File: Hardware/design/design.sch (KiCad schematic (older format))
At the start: 69 parts, among them SW1 NKK_NR01, SW10 NKK_NR01, SW11 SW_Push, SW12 SW_Push, SW13 SW_Push, SW14 SW_Push, SW15 NKK_NR01, SW16 SW_Push, SW17 SW_Push, SW18 SW_Push, SW19 SW_Push, SW2 SW_Push, SW20 NKK_NR01, SW21 SW_Push, SW22 SW_Push, SW23 SW_Push, SW24 SW_Push, SW25 SW_Push, SW26 SW_Push, SW27 SW_Push, SW28 SW_Push, SW3 SW_Push, SW4 SW_Push, SW5 SW_Push, SW6 SW_Push, SW7 SW_Push, SW8 SW_Push, SW9 SW_Push, U1 ProMicro

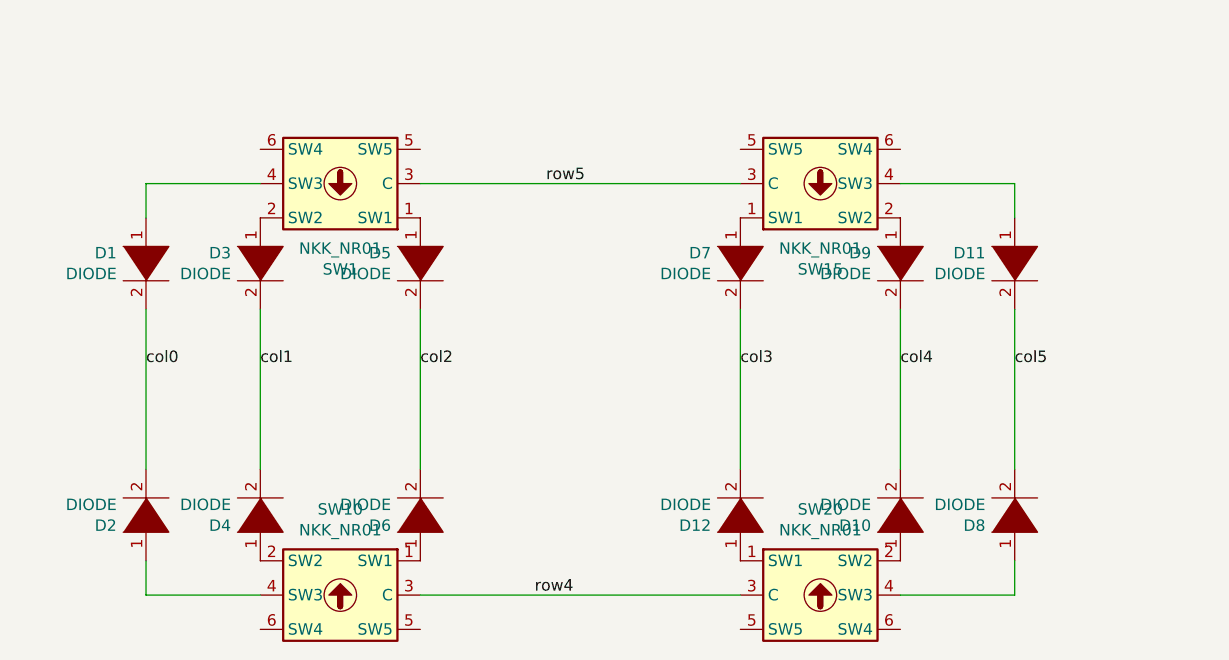
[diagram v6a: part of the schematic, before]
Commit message: routed all cherry switches and pots, fixed issue with rotary switch nets in schematic
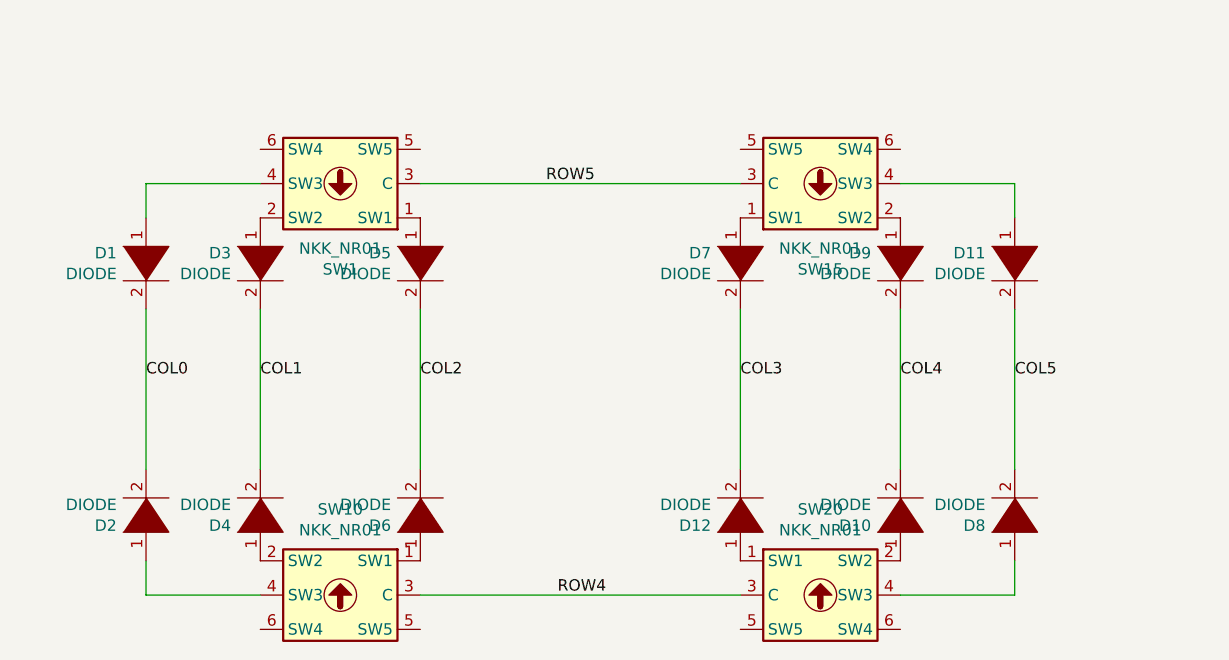
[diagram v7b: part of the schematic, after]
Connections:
- net labels removed: col0, col1, col2, col3, col4, col5, row4, row5
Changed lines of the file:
@@
 	1    0    0    -1
 $EndComp
-Text Label 3000 7100 0    50   ~ 0
-row4
 Wire Wire Line
 	5100 7100 5100 6950
@@
 	1300 5850 1300 6550
 Text Label 3050 5300 0    50   ~ 0
-row5
-Text Label 1300 6100 0    50   ~ 0
-col0
-Text Label 1800 6100 0    50   ~ 0
-col1
-Text Label 2500 6100 0    50   ~ 0
-col2
-Text Label 3900 6100 0    50   ~ 0
-col3
-Text Label 4600 6100 0    50   ~ 0
-col4
-Text Label 5100 6100 0    50   ~ 0
-col5
+ROW5
+Text Label 3100 7100 0    50   ~ 0
+ROW4
+Text Label 1300 6150 0    50   ~ 0
+COL0
+Text Label 1800 6150 0    50   ~ 0
+COL1
+Text Label 2500 6150 0    50   ~ 0
+COL2
+Text Label 3900 6150 0    50   ~ 0
+COL3
+Text Label 4600 6150 0    50   ~ 0
+COL4
+Text Label 5100 6150 0    50   ~ 0
+COL5
 $EndSCHEMATC

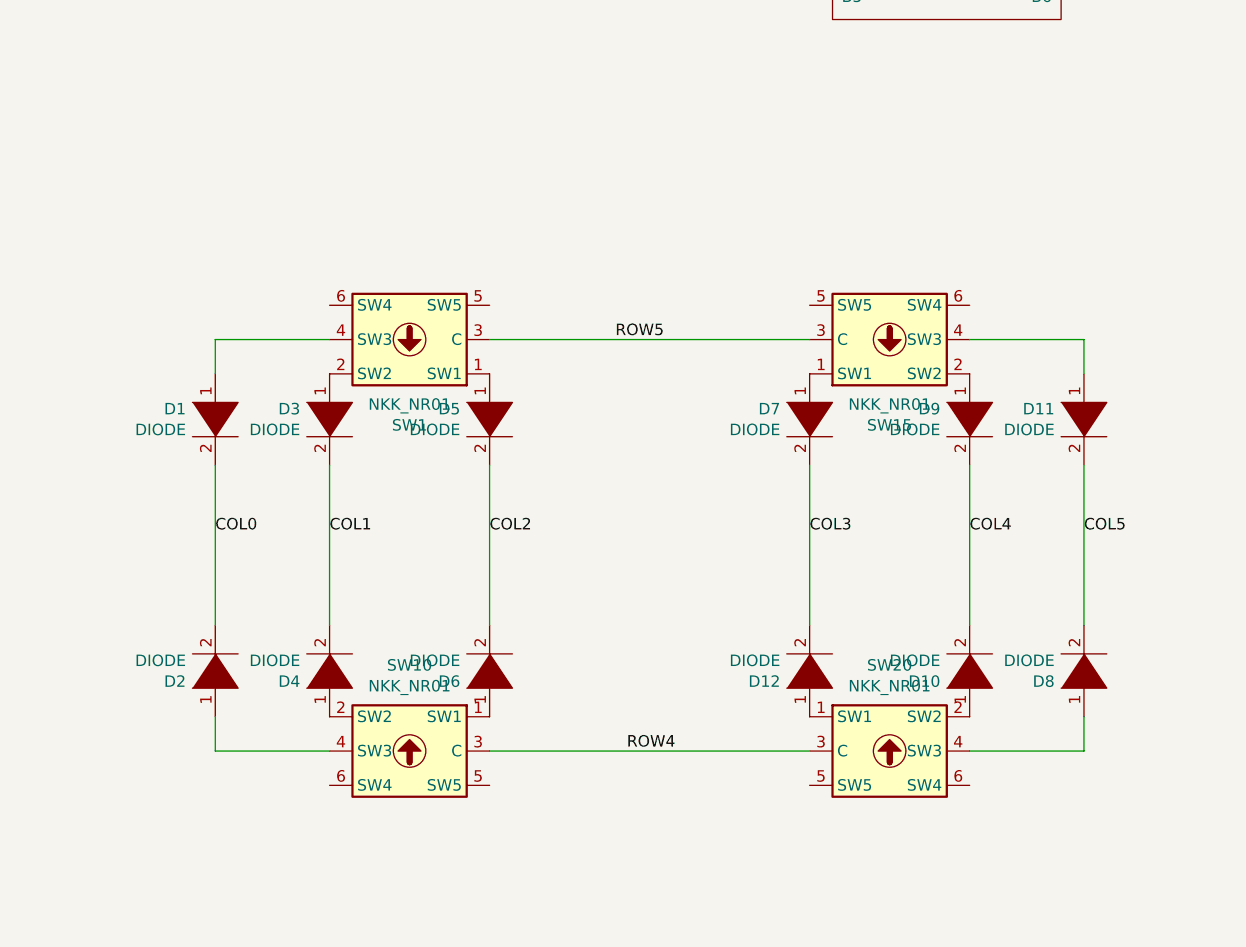
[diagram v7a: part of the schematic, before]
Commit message: changed from 4x3 rotary swithches to 2x6 rotary switches for octave control of each half of keyboard
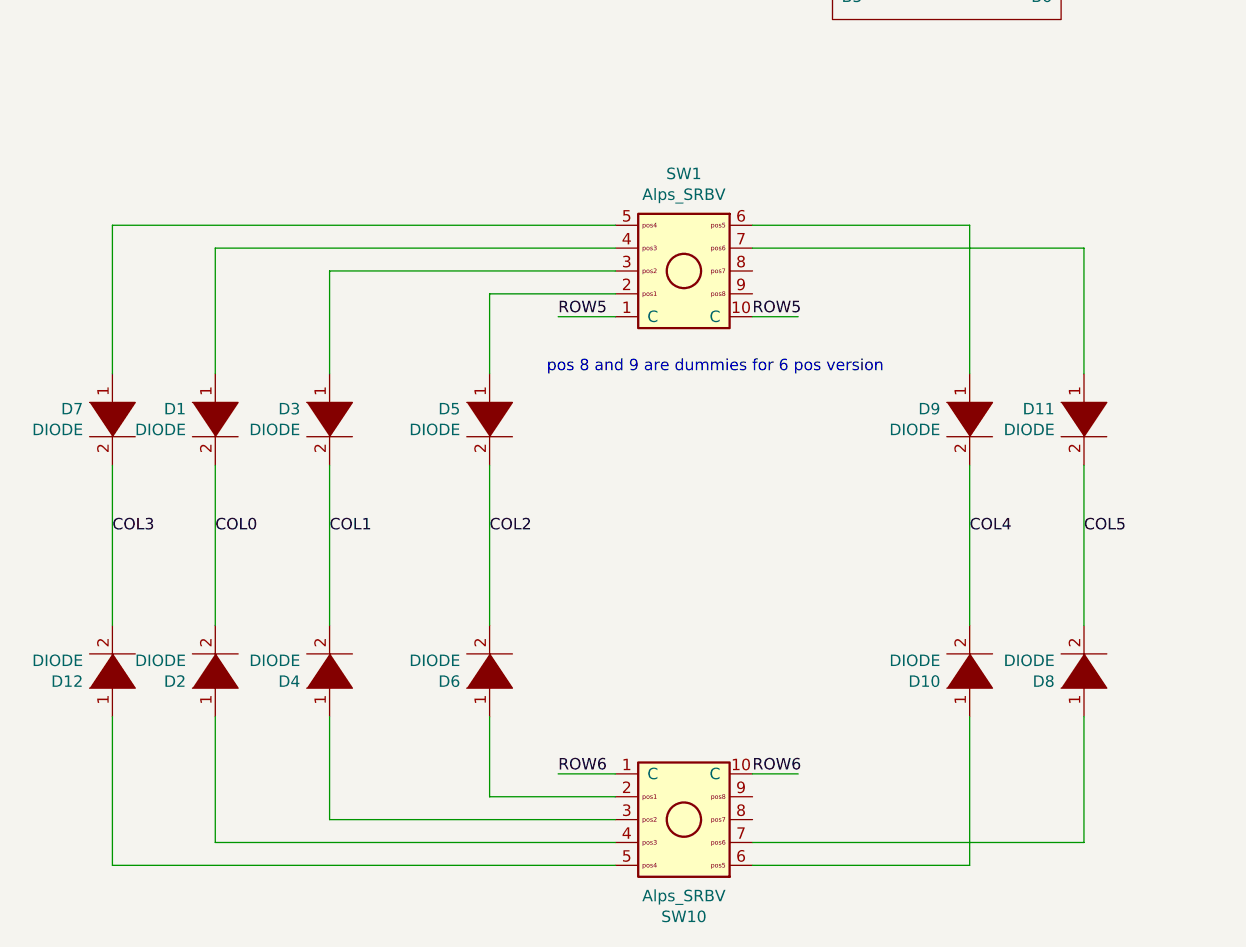
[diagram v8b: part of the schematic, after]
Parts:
- removed SW1, SW10, SW15, SW20: NKK_NR01, Kicad_Akiyuki_Footprint:NR01, symbol Akiyuki_UI:NKK_NR01
- added SW1, SW10: Alps_SRBV, Kicad_Akiyuki_Footprint:ALPS_SRBV, symbol Akiyuki_UI:Alps_SRBV
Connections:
- net labels added: ROW6
- wire segments 141 -> 159
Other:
- note added: "pos 8 and 9 are dummies for 6 pos version"
- moved on the sheet: D12, D7
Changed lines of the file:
@@
 Scanning process pseudocode:\n\nInit(){\nfor row in rows{\nsetmode(row, INPUT_PULLUP);\n}\nfor col in cols{\nsetmode(col, OUTPUT);\nwrite(col,1);\n} \n}\ndef scan_row(row){\nfor col in cols{\nwrite(col, 0);\nif(read(row) == 0){\n//button at (row,col) is pressed\n}\nwrite(col, 1);\n}\n}
-$Comp
-L Akiyuki_UI:NKK_NR01 SW10
-U 1 1 61648AD9
-P 2150 7100
-F 0 "SW10" H 2150 7475 50  0000 C CNN
-F 1 "NKK_NR01" H 2150 7384 50  0000 C CNN
-F 2 "Kicad_Akiyuki_Footprint:NR01" H 2125 7125 50  0001 C CNN
-F 3 "" H 2125 7125 50  0001 C CNN
-	1    2150 7100
-	1    0    0    -1
-$EndComp
-Wire Wire Line
-	5100 7100 5100 6950
 $Comp
 L pspice:DIODE D12
 U 1 1 61698380
-P 3900 6750
-F 0 "D12" V 3854 6878 50  0000 L CNN
-F 1 "DIODE" V 3945 6878 50  0000 L CNN
-F 2 "Diode_SMD:D_1206_3216Metric" H 3900 6750 50  0001 C CNN
-F 3 "~" H 3900 6750 50  0001 C CNN
-	1    3900 6750
+P 850 6750
+F 0 "D12" V 804 6878 50  0000 L CNN
+F 1 "DIODE" V 895 6878 50  0000 L CNN
+F 2 "Diode_SMD:D_1206_3216Metric" H 850 6750 50  0001 C CNN
+F 3 "~" H 850 6750 50  0001 C CNN
+	1    850  6750
 	0    -1   -1   0
 $EndComp
-$Comp
-L Akiyuki_UI:NKK_NR01 SW20
-U 1 1 61648ADF
-P 4250 7100
-F 0 "SW20" H 4250 7475 50  0000 C CNN
-F 1 "NKK_NR01" H 4250 7384 50  0000 C CNN
-F 2 "Kicad_Akiyuki_Footprint:NR01" H 4225 7125 50  0001 C CNN
-F 3 "" H 4225 7125 50  0001 C CNN
-	1    4250 7100
-	-1   0    0    -1
-$EndComp
-Wire Wire Line
-	2500 7100 3900 7100
 $Comp
 L pspice:DIODE D8
@@
 $EndComp
 Wire Wire Line
-	1800 7100 1300 7100
-Wire Wire Line
-	1300 7100 1300 6950
-Wire Wire Line
-	4600 7100 5100 7100
+	850  5850 850  6550
+Wire Wire Line
+	4600 5850 4600 6550
+Wire Wire Line
+	5100 5850 5100 6550
+Wire Wire Line
+	2500 5850 2500 6550
+Wire Wire Line
+	1800 5850 1800 6550
+Wire Wire Line
+	1300 5850 1300 6550
+Text Label 1300 6150 0    50   ~ 0
+COL0
+Text Label 1800 6150 0    50   ~ 0
+COL1
+Text Label 2500 6150 0    50   ~ 0
+COL2
+Text Label 850  6150 0    50   ~ 0
+COL3
+Text Label 4600 6150 0    50   ~ 0
+COL4
+Text Label 5100 6150 0    50   ~ 0
+COL5
+Wire Wire Line
+	3050 5200 2800 5200
+Wire Wire Line
+	3650 5200 3850 5200
+Text Notes 2750 5450 0    50   ~ 0
+pos 8 and 9 are dummies for 6 pos version
+Wire Wire Line
+	5100 4900 5100 5450
+Wire Wire Line
+	3650 4900 5100 4900
+Wire Wire Line
+	4600 4800 3650 4800
+Wire Wire Line
+	4600 5450 4600 4800
+Wire Wire Line
+	850  4800 850  5450
+Wire Wire Line
+	850  4800 3050 4800
+Wire Wire Line
+	1300 4900 1300 5450
+Wire Wire Line
+	1300 4900 3050 4900
+Wire Wire Line
+	1800 5000 3050 5000
+Wire Wire Line
+	1800 5450 1800 5000
+Wire Wire Line
+	2500 5100 2500 5450
+Wire Wire Line
+	3050 5100 2500 5100
+$Comp
+L Akiyuki_UI:Alps_SRBV SW1
+U 1 1 6152064E
+P 3350 5000
+F 0 "SW1" V 2925 5000 50  0000 C CNN
+F 1 "Alps_SRBV" V 3016 5000 50  0000 C CNN
+F 2 "Kicad_Akiyuki_Footprint:ALPS_SRBV" H 3250 5160 50  0001 C CNN
+F 3 "~" H 3350 5260 50  0001 C CNN
+	1    3350 5000
+	0    1    1    0
+$EndComp
+$Comp
+L pspice:DIODE D9
+U 1 1 616F9FD5
+P 4600 5650
+F 0 "D9" V 4554 5778 50  0000 L CNN
+F 1 "DIODE" V 4645 5778 50  0000 L CNN
+F 2 "Diode_SMD:D_1206_3216Metric" H 4600 5650 50  0001 C CNN
+F 3 "~" H 4600 5650 50  0001 C CNN
+	1    4600 5650
+	0    -1   1    0
+$EndComp
+$Comp
+L pspice:DIODE D11
+U 1 1 616F9FCF
+P 5100 5650
+F 0 "D11" V 5054 5778 50  0000 L CNN
+F 1 "DIODE" V 5145 5778 50  0000 L CNN
+F 2 "Diode_SMD:D_1206_3216Metric" H 5100 5650 50  0001 C CNN
+F 3 "~" H 5100 5650 50  0001 C CNN
+	1    5100 5650
+	0    -1   1    0
+$EndComp
+$Comp
+L pspice:DIODE D7
+U 1 1 616F9FC2
+P 850 5650
+F 0 "D7" V 804 5778 50  0000 L CNN
+F 1 "DIODE" V 895 5778 50  0000 L CNN
+F 2 "Diode_SMD:D_1206_3216Metric" H 850 5650 50  0001 C CNN
+F 3 "~" H 850 5650 50  0001 C CNN
+	1    850  5650
+	0    -1   1    0
+$EndComp
+$Comp
+L pspice:DIODE D5
+U 1 1 616F9FB4
+P 2500 5650
+F 0 "D5" V 2454 5778 50  0000 L CNN
+F 1 "DIODE" V 2545 5778 50  0000 L CNN
+F 2 "Diode_SMD:D_1206_3216Metric" H 2500 5650 50  0001 C CNN
+F 3 "~" H 2500 5650 50  0001 C CNN
+	1    2500 5650
+	0    -1   1    0
+$EndComp
+$Comp
+L pspice:DIODE D1
+U 1 1 616F9FAE
+P 1300 5650
+F 0 "D1" V 1254 5778 50  0000 L CNN
+F 1 "DIODE" V 1345 5778 50  0000 L CNN
+F 2 "Diode_SMD:D_1206_3216Metric" H 1300 5650 50  0001 C CNN
+F 3 "~" H 1300 5650 50  0001 C CNN
+	1    1300 5650
+	0    -1   1    0
+$EndComp
 $Comp
 L pspice:DIODE D3
@@
 	0    -1   1    0
 $EndComp
-$Comp
-L pspice:DIODE D1
-U 1 1 616F9FAE
-P 1300 5650
-F 0 "D1" V 1254 5778 50  0000 L CNN
-F 1 "DIODE" V 1345 5778 50  0000 L CNN
-F 2 "Diode_SMD:D_1206_3216Metric" H 1300 5650 50  0001 C CNN
-F 3 "~" H 1300 5650 50  0001 C CNN
-	1    1300 5650
-	0    -1   1    0
-$EndComp
-$Comp
-L pspice:DIODE D5
-U 1 1 616F9FB4
-P 2500 5650
-F 0 "D5" V 2454 5778 50  0000 L CNN
-F 1 "DIODE" V 2545 5778 50  0000 L CNN
-F 2 "Diode_SMD:D_1206_3216Metric" H 2500 5650 50  0001 C CNN
-F 3 "~" H 2500 5650 50  0001 C CNN
-	1    2500 5650
-	0    -1   1    0
-$EndComp
-$Comp
-L Akiyuki_UI:NKK_NR01 SW1
-U 1 1 616F9FBA
-P 2150 5300
-F 0 "SW1" H 2150 5675 50  0000 C CNN
-F 1 "NKK_NR01" H 2150 5584 50  0000 C CNN
-F 2 "Kicad_Akiyuki_Footprint:NR01" H 2125 5325 50  0001 C CNN
-F 3 "" H 2125 5325 50  0001 C CNN
-	1    2150 5300
-	1    0    0    1
-$EndComp
-Wire Wire Line
-	5100 5300 5100 5450
-$Comp
-L pspice:DIODE D7
-U 1 1 616F9FC2
-P 3900 5650
-F 0 "D7" V 3854 5778 50  0000 L CNN
-F 1 "DIODE" V 3945 5778 50  0000 L CNN
-F 2 "Diode_SMD:D_1206_3216Metric" H 3900 5650 50  0001 C CNN
-F 3 "~" H 3900 5650 50  0001 C CNN
-	1    3900 5650
-	0    -1   1    0
-$EndComp
-$Comp
-L Akiyuki_UI:NKK_NR01 SW15
-U 1 1 616F9FC8
-P 4250 5300
-F 0 "SW15" H 4250 5675 50  0000 C CNN
-F 1 "NKK_NR01" H 4250 5584 50  0000 C CNN
-F 2 "Kicad_Akiyuki_Footprint:NR01" H 4225 5325 50  0001 C CNN
-F 3 "" H 4225 5325 50  0001 C CNN
-	1    4250 5300
-	-1   0    0    1
-$EndComp
-Wire Wire Line
-	2500 5300 3900 5300
-$Comp
-L pspice:DIODE D11
-U 1 1 616F9FCF
-P 5100 5650
-F 0 "D11" V 5054 5778 50  0000 L CNN
-F 1 "DIODE" V 5145 5778 50  0000 L CNN
-F 2 "Diode_SMD:D_1206_3216Metric" H 5100 5650 50  0001 C CNN
-F 3 "~" H 5100 5650 50  0001 C CNN
-	1    5100 5650
-	0    -1   1    0
-$EndComp
-$Comp
-L pspice:DIODE D9
-U 1 1 616F9FD5
-P 4600 5650
-F 0 "D9" V 4554 5778 50  0000 L CNN
-F 1 "DIODE" V 4645 5778 50  0000 L CNN
-F 2 "Diode_SMD:D_1206_3216Metric" H 4600 5650 50  0001 C CNN
-F 3 "~" H 4600 5650 50  0001 C CNN
-	1    4600 5650
-	0    -1   1    0
-$EndComp
-Wire Wire Line
-	1800 5300 1300 5300
-Wire Wire Line
-	1300 5300 1300 5450
-Wire Wire Line
-	4600 5300 5100 5300
-Wire Wire Line
-	3900 5850 3900 6550
-Wire Wire Line
-	4600 5850 4600 6550
-Wire Wire Line
-	5100 5850 5100 6550
-Wire Wire Line
-	2500 5850 2500 6550
-Wire Wire Line
-	1800 5850 1800 6550
-Wire Wire Line
-	1300 5850 1300 6550
-Text Label 3050 5300 0    50   ~ 0
+Wire Wire Line
+	3050 7200 2800 7200
+Wire Wire Line
+	3650 7200 3850 7200
+Wire Wire Line
+	5100 7500 5100 6950
+Wire Wire Line
+	3650 7500 5100 7500
+Wire Wire Line
+	4600 7600 3650 7600
+Wire Wire Line
+	4600 6950 4600 7600
+Wire Wire Line
+	850  7600 850  6950
+Wire Wire Line
+	850  7600 3050 7600
+Wire Wire Line
+	1300 7500 1300 6950
+Wire Wire Line
+	1300 7500 3050 7500
+Wire Wire Line
+	1800 7400 3050 7400
+Wire Wire Line
+	1800 6950 1800 7400
+Wire Wire Line
+	2500 7300 2500 6950
+Wire Wire Line
+	3050 7300 2500 7300
+$Comp
+L Akiyuki_UI:Alps_SRBV SW10
+U 1 1 6159FC58
+P 3350 7400
+F 0 "SW10" V 2925 7400 50  0000 C CNN
+F 1 "Alps_SRBV" V 3016 7400 50  0000 C CNN
+F 2 "Kicad_Akiyuki_Footprint:ALPS_SRBV" H 3250 7560 50  0001 C CNN
+F 3 "~" H 3350 7660 50  0001 C CNN
+	1    3350 7400
+	0    1    -1   0
+$EndComp
+Text Label 3650 7200 0    50   ~ 0
+ROW6
+Text Label 2800 7200 0    50   ~ 0
+ROW6
+Text Label 2800 5200 0    50   ~ 0
 ROW5
-Text Label 3100 7100 0    50   ~ 0
-ROW4
-Text Label 1300 6150 0    50   ~ 0
-COL0
-Text Label 1800 6150 0    50   ~ 0
-COL1
-Text Label 2500 6150 0    50   ~ 0
-COL2
-Text Label 3900 6150 0    50   ~ 0
-COL3
-Text Label 4600 6150 0    50   ~ 0
-COL4
-Text Label 5100 6150 0    50   ~ 0
-COL5
+Text Label 3650 5200 0    50   ~ 0
+ROW5
 $EndSCHEMATC
